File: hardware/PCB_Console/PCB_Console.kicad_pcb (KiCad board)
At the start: 2 copper layers, 100 x 150 mm, 63 parts, among them J1 USB_C_Receptacle_PowerOnly_6P, J2 CP2102 module, Q1 2N3904, Q2 2N3904, SW1 SW_MEC_5E, SW2 SW_MEC_5E, SW3 SW_MEC_5E, SW4 SW_MEC_5E, SW5 SW_MEC_5E, SW6 SW_MEC_5E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

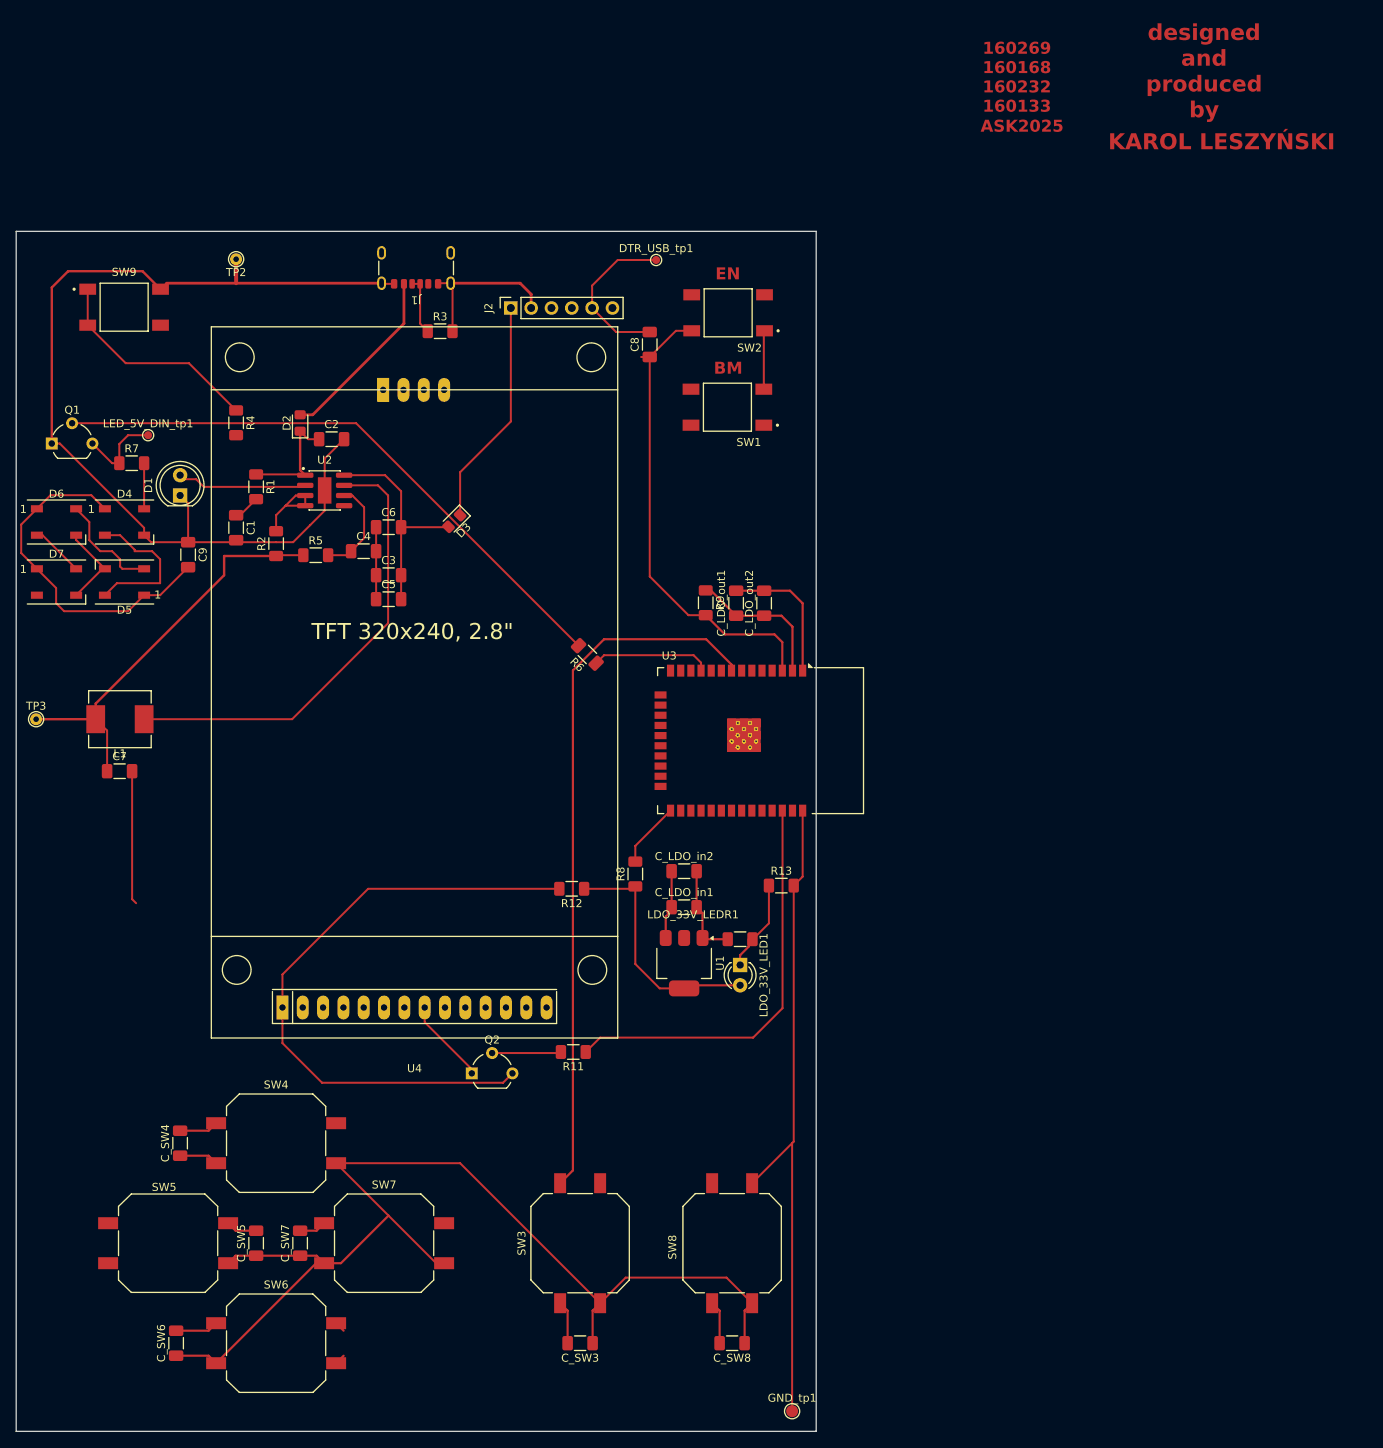
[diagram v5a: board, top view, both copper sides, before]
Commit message: routing on 2l done, need to check, text and logo added
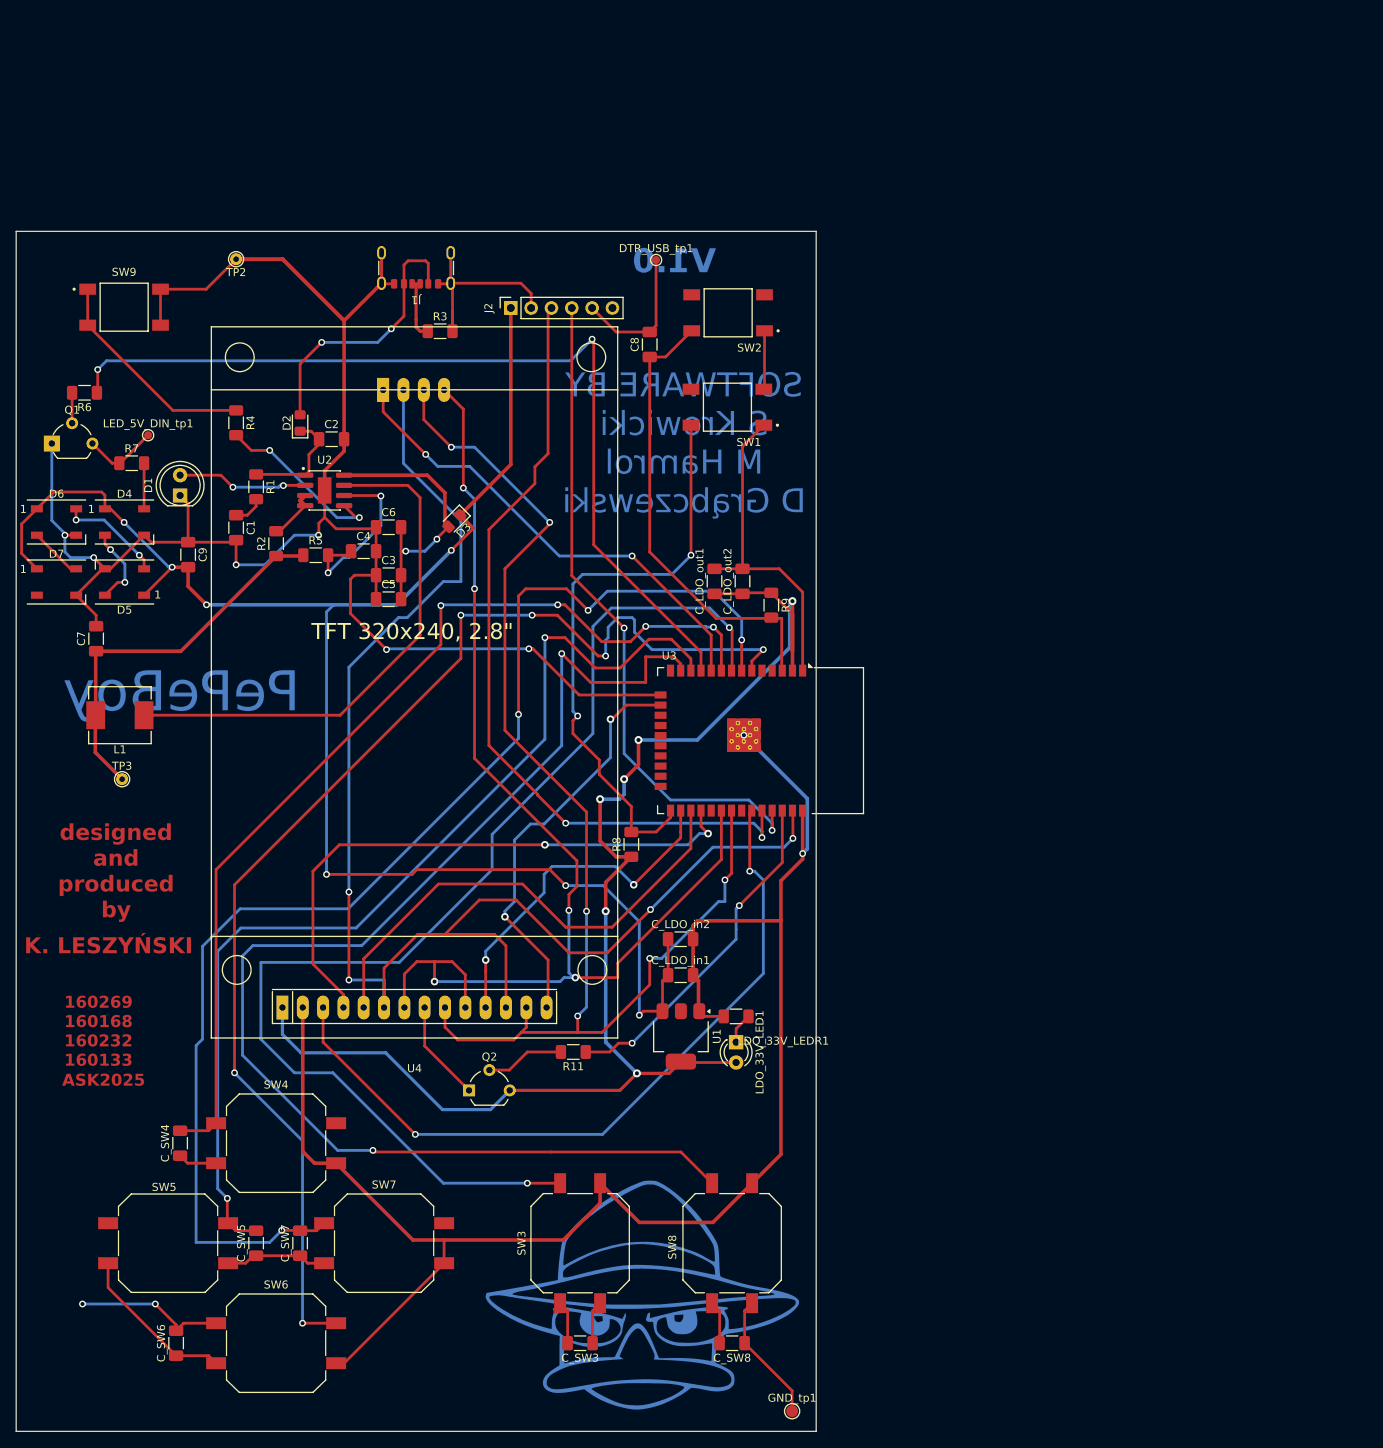
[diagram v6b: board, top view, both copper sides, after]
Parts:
- removed R12, R13: 0, Resistor_SMD:R_1206_3216Metric_Pad1.30x1.75mm_HandSolder
- added G***: LOGO, LOGO, B.Cu at (128.5, 158.5)
- moved R6 70.9 mm to (58.5, 45.2), turned to 180 degrees
- moved C7 16.8 mm to (60.0, 75.9), turned to 90 degrees
- moved TP3 13.1 mm to (63.2, 93.5)
- moved LDO_33V_LED1 9.66 mm to (140.0, 126.4)
- moved LDO_33V_LEDR1 9.66 mm to (140.0, 123.1), turned to 180 degrees
- moved U1 9.16 mm to (133.1, 125.6)
- moved C_LDO_in1 8.51 mm to (133.1, 118.0)
- moved C_LDO_in2 8.51 mm to (133.1, 113.5)
- moved R9 8.21 mm to (144.4, 71.7)
- moved C_LDO_out1 3.84 mm to (137.3, 68.7)
- moved C_LDO_out2 3.84 mm to (140.8, 68.7)
- moved R8 3.73 mm to (126.9, 101.6)
- moved Q2 2.16 mm to (106.6, 132.4)
- moved L1 0.50 mm to (63.0, 85.5)
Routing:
- net SPI_MOSI: track 0.00 -> 179.9 mm, vias 0 -> 4
- net IO34_B: track 6.71 -> 176.5 mm, vias 0 -> 8
- net IO14_B: track 5.39 -> 166.2 mm, vias 0 -> 2
- net SPI_MISO: track 0.00 -> 157.8 mm, vias 0 -> 6
- net IO35_B: track 3.39 -> 160.7 mm, vias 0 -> 4
- net SPI_SCK: track 0.00 -> 150.3 mm, vias 0 -> 5
- net 5V_USB_BL: track 80.7 -> 212.7 mm, vias 0 -> 7
- net IO27_B: track 3.89 -> 126.8 mm, vias 0 -> 2
- net IO33_B: track 4.89 -> 123.9 mm, vias 0 -> 4
- net TXD_USB: track 0.00 -> 100.7 mm, vias 0 -> 2
- net IC_LED_DIN: track 14.9 -> 113.4 mm, vias 0 -> 2
- net Bat-: track 452.6 -> 546.9 mm, vias 0 -> 8
- net SPI_CS_D: track 0.00 -> 94.0 mm, vias 0 -> 2
- net RXD_USB: track 0.00 -> 83.9 mm, vias 0 -> 2
- net D_RST: track 0.00 -> 73.2 mm, vias 0 -> 2
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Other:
- board text added: "K. LESZYŃSKI"
- board text added: "PePeBoy"
- board text added: "SOFTWARE BY S Krowicki M Hamrol D Grąbczewski"
- board text added: "V1.0"
- board text removed: "BM"
- board text removed: "EN"
- board text removed: "KAROL LESZYŃSKI"

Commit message: pcb that was produced
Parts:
- moved R3 74.1 mm to (33.0, 13.0), turned to 180 degrees
- moved J1 69.4 mm to (35.3, 3.42)
- moved GND_tp1 65.5 mm to (87.5, 145.0)
- moved TP2 61.5 mm to (21.5, 3.00)
- moved C_LDO_in1 55.9 mm to (83.1, 93.0)
- moved C_LDO_in2 55.9 mm to (83.1, 88.5)
- moved LDO_33V_LED1 55.9 mm to (90.0, 101.4)
- moved C7 55.9 mm to (10.0, 50.9)
- moved C_SW8 55.9 mm to (89.5, 139.0)
- moved DTR_USB_tp1 55.9 mm to (80.0, 3.60)
- moved G*** 55.9 mm to (78.5, 133.5)
- moved L1 55.9 mm to (13.0, 60.5)
- moved LDO_33V_LEDR1 55.9 mm to (90.0, 98.2)
- moved Q1 55.9 mm to (4.47, 26.5)
- moved SW2 55.9 mm to (89.0, 10.2)
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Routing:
- net Net-(D2-A): track 34.2 -> 17.3 mm, vias 2 -> 0
- net 3_3V_AMSVO: track 171.4 -> 164.2 mm
- net SPI_MOSI: track 179.9 -> 186.9 mm
- net D_RST: track 73.2 -> 74.9 mm
- net SPI_CS_D: track 94.0 -> 95.3 mm
- net TXD_USB: track 100.7 -> 101.9 mm
- net Bat-: track 546.9 -> 546.1 mm
- net RXD_USB: track 83.9 -> 83.1 mm
- net 5V_USB_BL: track 212.7 -> 213.3 mm
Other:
- outline, holes or cut-outs redrawn
